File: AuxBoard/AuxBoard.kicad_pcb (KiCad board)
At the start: 2 copper layers, 85.2 x 59.2 mm, 18 parts, among them J1 ATX-24, J10 MatBIn, J11 FanHeader, J2 RPI4B, J3 Passthrough, J4 MatrixASupply, J5 MatrixBSupply, J6 BigLED, J7 MatAOut, J8 MatAIn, J9 MatBOut, U1 74125

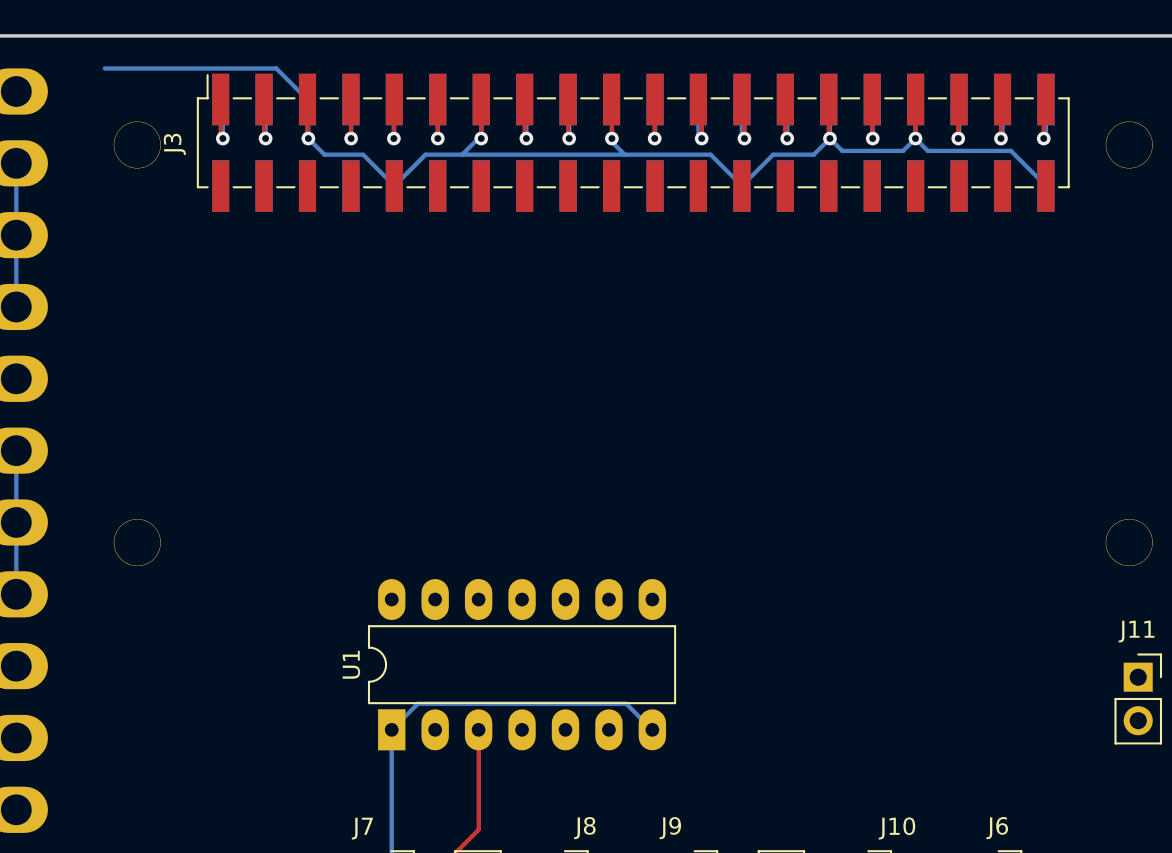
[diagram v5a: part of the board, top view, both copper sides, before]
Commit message: Simulated Ideal Diode to check functionality. Swaped Tristate buffer for hex inverter. Swapped to passthrough footprint.
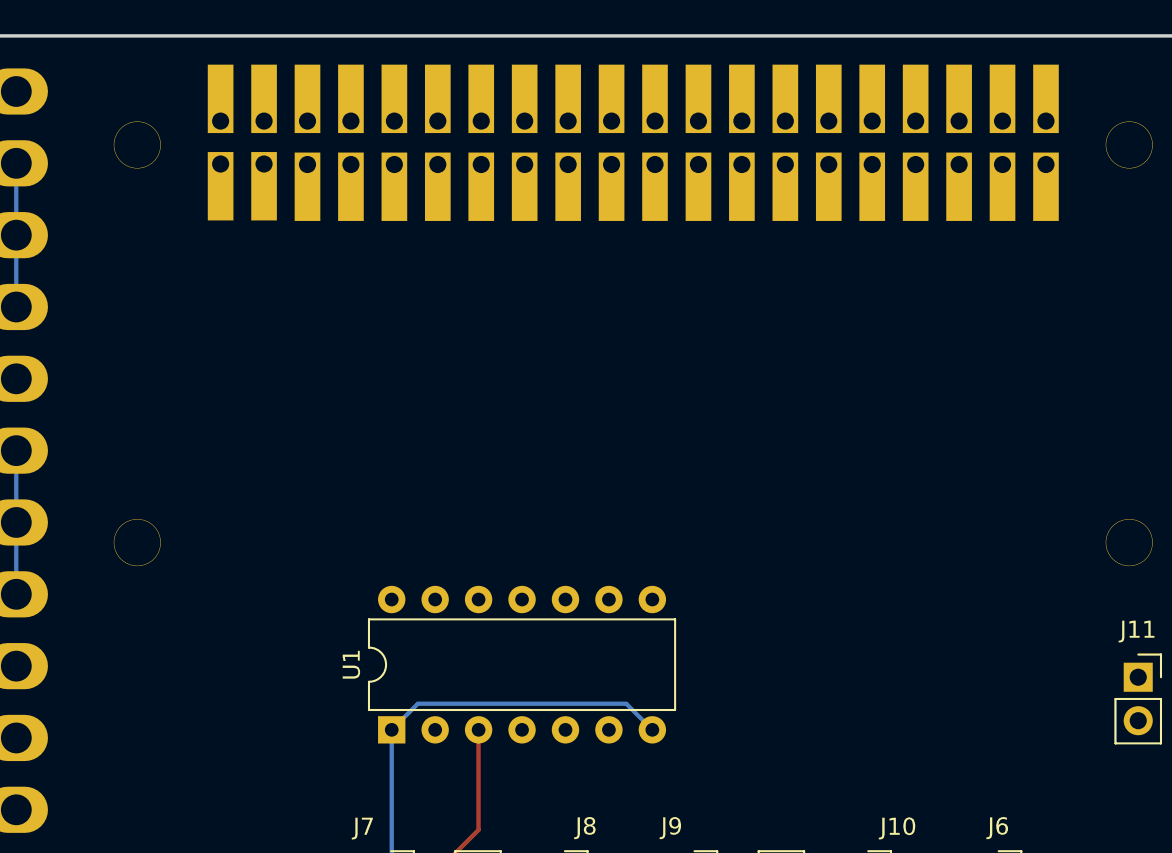
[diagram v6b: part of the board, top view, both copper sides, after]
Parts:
- removed J3: Passthrough, Connector_PinSocket_2.54mm:PinSocket_2x20_P2.54mm_FLIPED_Vertical_SMD
- J2: footprint Connector_PinSocket_2.54mm:PinSocket_2x20_P2.54mm_Vertical_SMD -> Tom's Parts:PI Header Passthrough
- U1: value 74125 -> 74AHC04; footprint Package_DIP:DIP-14_W7.62mm_LongPads -> Package_DIP:DIP-14_W7.62mm
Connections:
- U1 pad 1: GND -> /MOSI
- U1 pad 2: /MOSI -> Net-(U1-Pad2)
- U1 pad 3: DOUT -> Net-(U1-Pad2)
- U1 pad 4: unconnected-(U1B-EN-Pad4) -> DOUT
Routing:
- net GND: track 205.3 -> 118.4 mm, vias 5 -> 0
- net /5V_Power: track 9.30 -> 0.00 mm, vias 2 -> 0
- net /GPIO_8: track 4.72 -> 0.00 mm, vias 1 -> 0
- net /GPIO_7: track 4.68 -> 0.00 mm, vias 1 -> 0
- net /GPIO_21: track 4.67 -> 0.00 mm, vias 1 -> 0
- net /GPIO_1: track 4.65 -> 0.00 mm, vias 1 -> 0
- net /GPIO_23: track 4.64 -> 0.00 mm, vias 1 -> 0
- net /GPIO_20: track 4.63 -> 0.00 mm, vias 1 -> 0
- net /GPIO_24: track 4.61 -> 0.00 mm, vias 1 -> 0
- net /GPIO_16: track 4.60 -> 0.00 mm, vias 1 -> 0
- net /GPIO_15: track 4.58 -> 0.00 mm, vias 1 -> 0
- net /GPIO_12: track 4.58 -> 0.00 mm, vias 1 -> 0
- net /GPIO_25: track 4.58 -> 0.00 mm, vias 1 -> 0
- net /GPIO_14: track 4.57 -> 0.00 mm, vias 1 -> 0
- net /GPIO_18: track 4.56 -> 0.00 mm, vias 1 -> 0

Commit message: Final PCB Layout
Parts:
- removed REF** (x6): MountingHole_2.75mm_RPI_HAT, MountingHole:MountingHole_2.75mm_RPI_HAT
- added H1: MountingHole, Tom's Parts:MountingHole_2.75mm_RPI_HAT, F.Cu at (128.5, 105.4)
- added H2: MountingHole, Tom's Parts:MountingHole_2.75mm_RPI_HAT, F.Cu at (128.5, 79.4)
- added H3: MountingHole, Tom's Parts:MountingHole_2.75mm_RPI_HAT, F.Cu at (186.5, 105.4)
- added H4: MountingHole, Tom's Parts:MountingHole_2.75mm_RPI_HAT, F.Cu at (186.5, 79.4)
- added H5: MountingHole, Tom's Parts:MountingHole_2.75mm_RPI_HAT, F.Cu at (128.5, 56.1)
- added H6: MountingHole, Tom's Parts:MountingHole_2.75mm_RPI_HAT, F.Cu at (186.5, 56.1)
- added PolyFuse2: 5A, Fuse:Fuse_2920_7451Metric_Pad2.10x5.45mm_HandSolder, F.Cu at (142.8, 89.0)
- added PolyFuse3: 5A, Fuse:Fuse_2920_7451Metric_Pad2.10x5.45mm_HandSolder, F.Cu at (160.4, 89.0)
- added PolyFuse4: 3A, Fuse:Fuse_2920_7451Metric_Pad2.10x5.45mm_HandSolder, F.Cu at (176.7, 89.0)
- added PolyFuse5: 2A, Fuse:Fuse_1812_4532Metric_Pad1.30x3.40mm_HandSolder, F.Cu at (137.8, 73.1)
- added Q1: DMMT5401, Package_TO_SOT_SMD:SOT-23-6, F.Cu at (147.2, 68.2)
- added Q2: DMG2305UX, Package_TO_SOT_SMD:SOT-23-3, F.Cu at (147.2, 64.5)
- added Q3: DMG2305UX, Package_TO_SOT_SMD:SOT-23-3, F.Cu at (133.8, 68.1)
- added Q4: DMG2305UX, Package_TO_SOT_SMD:SOT-23-3, F.Cu at (186.9, 96.6)
- added R1: 10K, Resistor_SMD:R_0805_2012Metric_Pad1.20x1.40mm_HandSolder, F.Cu at (138.5, 68.2)
- added R2: 47K, Resistor_SMD:R_0805_2012Metric_Pad1.20x1.40mm_HandSolder, F.Cu at (140.5, 68.2)
- added R3: 10K, Resistor_SMD:R_0805_2012Metric_Pad1.20x1.40mm_HandSolder, F.Cu at (136.6, 68.2)
- added SW1: SW_DPST, Connector_PinHeader_2.54mm:PinHeader_2x02_P2.54mm_Vertical, F.Cu at (106.8, 104.4)
- moved U1 13.8 mm to (151.0, 78.8)
- moved J10 7.99 mm to (164.4, 102.8), turned to 180 degrees
- moved J8 7.57 mm to (147.1, 102.8), turned to 180 degrees
- moved J9 6.54 mm to (156.0, 102.8), turned to 180 degrees
- moved J7 6.49 mm to (138.3, 102.8), turned to 180 degrees
- moved J5 6.01 mm to (160.2, 100.3), turned to 0 degrees
- moved J4 5.74 mm to (142.8, 100.3), turned to 0 degrees
- moved J6 4.64 mm to (176.7, 102.8), turned to 180 degrees
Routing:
- net /5VSwitch: track 0.00 -> 207.1 mm, vias 0 -> 2
- net GND: track 118.4 -> 278.1 mm, vias 0 -> 1
- net +12V: track 4.20 -> 153.1 mm, vias 0 -> 2
- net +5V: track 33.5 -> 125.7 mm, vias 0 -> 1
- net DOUT: track 13.1 -> 51.6 mm
- net Net-(J1-PS_ON#): track 0.00 -> 35.4 mm
- net /5V_Power: track 0.00 -> 27.3 mm, vias 0 -> 2
- net +5VP: track 0.00 -> 26.7 mm
- net /3V3_Power: track 0.00 -> 26.3 mm
- net /MOSI: track 0.00 -> 26.2 mm
- net 5VSB: track 0.00 -> 22.9 mm, vias 0 -> 1
- net Net-(Q1A-E1): track 0.00 -> 20.4 mm
- net Net-(Q1B-C2): track 0.00 -> 14.1 mm
- net Net-(Q1A-B1): track 0.00 -> 10.5 mm
- net 5VMatA: track 12.3 -> 22.1 mm
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
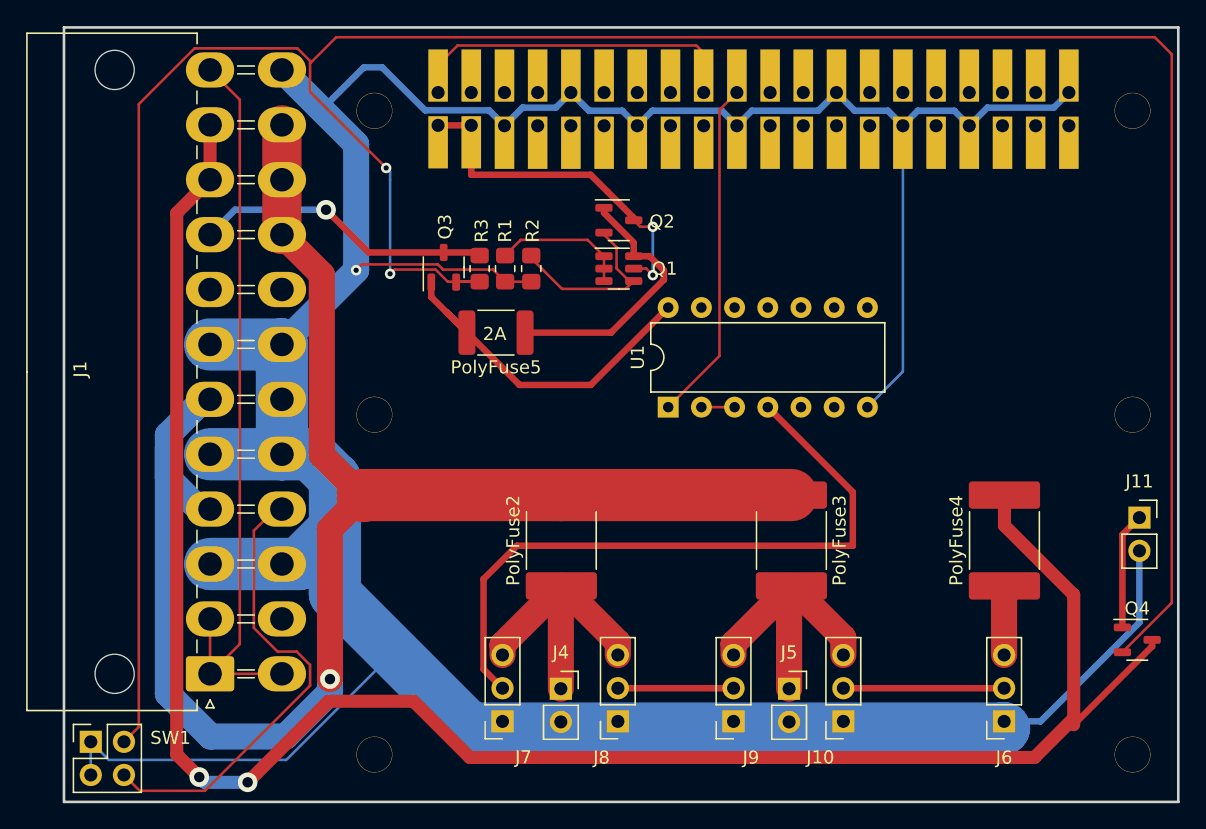
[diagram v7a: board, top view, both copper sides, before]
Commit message: Filled GND Net. Fixed most 3d elements
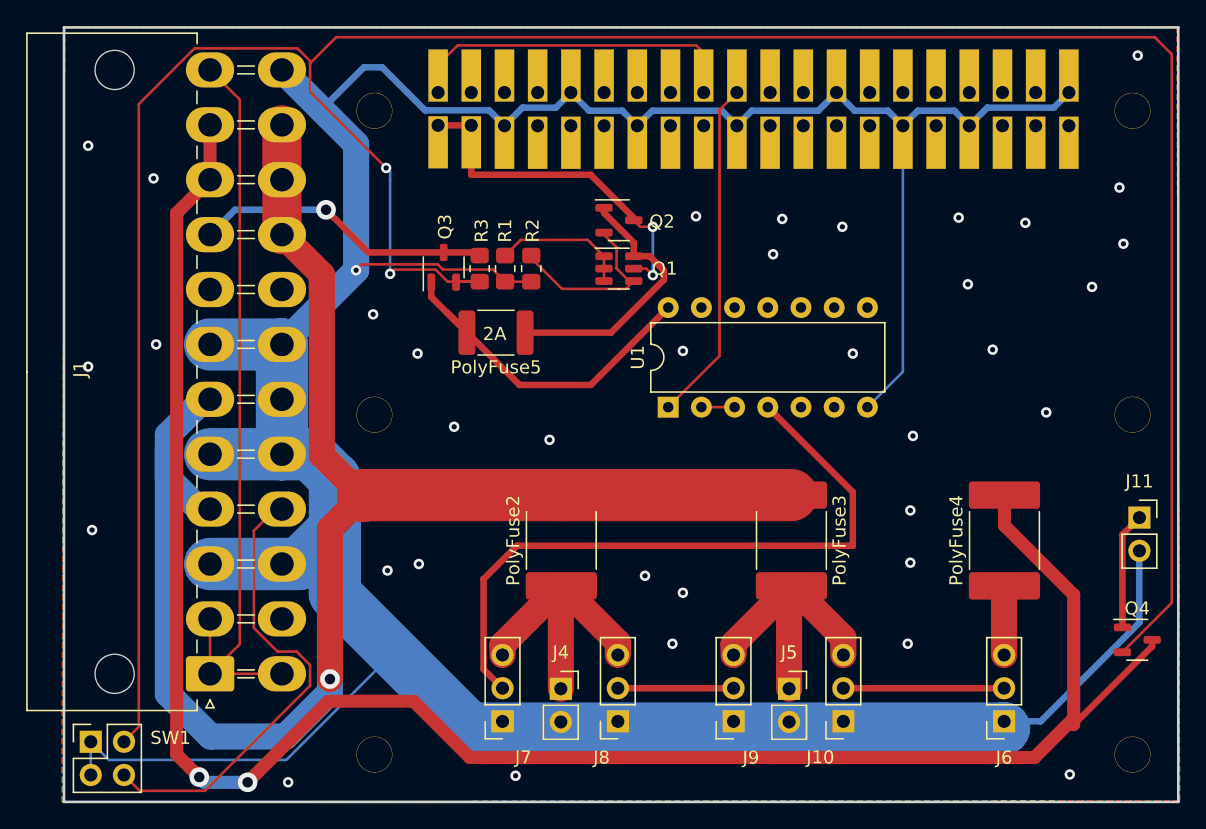
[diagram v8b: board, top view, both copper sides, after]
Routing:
- net GND: vias 1 -> 37
- added copper zone on B.Cu, net GND
- added copper zone on F.Cu, net GND
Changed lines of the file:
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@@
     (pad "2" smd roundrect (at 2.225 0 180) (size 1.3 3.4) (layers "F.Cu" "F.Paste" "F.Mask") (roundrect_rratio 0.192308)
       (net 49 "+5VP") (pintype "passive"))
-    (model "${KICAD6_3DMODEL_DIR}/Fuse.3dshapes/Fuse_1812_4532Metric.wrl"
+    (model "${KICAD7_3DMODEL_DIR}/Fuse.3dshapes/Fuse_1210_3225Metric.wrl"
       (offset (xyz 0 0 0))
       (scale (xyz 1 1 1))
@@
         (effects (font (size 1 1) (thickness 0.15)))
     )
-    (fp_text user "${REFERENCE}" (at 0 0 -90) (layer "F.Fab")
+    (fp_text user "${REFERENCE}" (at 0 0 90) (layer "F.Fab")
         (effects (font (size 1 1) (thickness 0.15)))
     )
@@
     (pad "2" smd roundrect (at 3.475 0 270) (size 2.1 5.45) (layers "F.Cu" "F.Paste" "F.Mask") (roundrect_rratio 0.119048)
       (net 46 "5VMatB") (pintype "passive"))
-    (model "${KICAD6_3DMODEL_DIR}/Fuse.3dshapes/Fuse_2920_7451Metric.wrl"
+    (model "${KICAD7_3DMODEL_DIR}/Fuse.3dshapes/Fuse_1210_3225Metric.wrl"
       (offset (xyz 0 0 0))
       (scale (xyz 1 1 1))
@@
     (pad "3" smd roundrect (at 1.1375 0) (size 1.325 0.6) (layers "F.Cu" "F.Paste" "F.Mask") (roundrect_rratio 0.25)
       (net 6 "/5V_Power") (pinfunction "S") (pintype "passive"))
-    (model "${KICAD6_3DMODEL_DIR}/Package_TO_SOT_SMD.3dshapes/SOT-23-3.wrl"
+    (model "${KICAD6_3DMODEL_DIR}/Package_TO_SOT_SMD.3dshapes/SOT-23.wrl"
       (offset (xyz 0 0 0))
       (scale (xyz 1 1 1))
@@
     (pad "3" smd roundrect (at 1.1375 0 90) (size 1.325 0.6) (layers "F.Cu" "F.Paste" "F.Mask") (roundrect_rratio 0.25)
       (net 32 "5VSB") (pinfunction "S") (pintype "passive"))
-    (model "${KICAD6_3DMODEL_DIR}/Package_TO_SOT_SMD.3dshapes/SOT-23-3.wrl"
+    (model "${KICAD6_3DMODEL_DIR}/Package_TO_SOT_SMD.3dshapes/SOT-23.wrl"
       (offset (xyz 0 0 0))
       (scale (xyz 1 1 1))
@@
     (pad "2" smd roundrect (at 3.475 0 90) (size 2.1 5.45) (layers "F.Cu" "F.Paste" "F.Mask") (roundrect_rratio 0.119048)
       (net 33 "+12V") (pintype "passive"))
-    (model "${KICAD6_3DMODEL_DIR}/Fuse.3dshapes/Fuse_2920_7451Metric.wrl"
+    (model "${KICAD7_3DMODEL_DIR}/Fuse.3dshapes/Fuse_1210_3225Metric.wrl"
       (offset (xyz 0 0 0))
       (scale (xyz 1 1 1))
@@
     (pad "2" smd roundrect (at 3.475 0 90) (size 2.1 5.45) (layers "F.Cu" "F.Paste" "F.Mask") (roundrect_rratio 0.119048)
       (net 30 "+5V") (pintype "passive"))
-    (model "${KICAD6_3DMODEL_DIR}/Fuse.3dshapes/Fuse_2920_7451Metric.wrl"
+    (model "${KICAD7_3DMODEL_DIR}/Fuse.3dshapes/Fuse_1210_3225Metric.wrl"
       (offset (xyz 0 0 0))
       (scale (xyz 1 1 1))
@@
     (pad "3" smd roundrect (at 1.1375 0) (size 1.325 0.6) (layers "F.Cu" "F.Paste" "F.Mask") (roundrect_rratio 0.25)
       (net 33 "+12V") (pinfunction "S") (pintype "passive"))
-    (model "${KICAD6_3DMODEL_DIR}/Package_TO_SOT_SMD.3dshapes/SOT-23-3.wrl"
+    (model "${KICAD7_3DMODEL_DIR}/Package_TO_SOT_SMD.3dshapes/SOT-23.wrl"
       (offset (xyz 0 0 0))
       (scale (xyz 1 1 1))
@@
   (segment (start 127.549501 67.875499) (end 127.1 68.325) (width 0.2) (layer "F.Cu") (net 48))
   (segment (start 138.5 69.2) (end 137.575 68.275) (width 0.2) (layer "F.Cu") (net 48))
+  (via (at 178.3 64.7) (size 0.8) (drill 0.4) (layers "F.Cu" "B.Cu") (free) (net 48))
+  (via (at 181.7 106.9) (size 0.8) (drill 0.4) (layers "F.Cu" "B.Cu") (free) (net 48))
+  (via (at 169.5 90.7) (size 0.8) (drill 0.4) (layers "F.Cu" "B.Cu") (free) (net 48))
+  (via (at 183.4 69.6) (size 0.8) (drill 0.4) (layers "F.Cu" "B.Cu") (free) (net 48))
+  (via (at 134.6 80.3) (size 0.8) (drill 0.4) (layers "F.Cu" "B.Cu") (free) (net 48))
   (via (at 127.1 68.325) (size 0.8) (drill 0.4) (layers "F.Cu" "B.Cu") (net 48))
+  (via (at 131.9 90.8) (size 0.8) (drill 0.4) (layers "F.Cu" "B.Cu") (free) (net 48))
+  (via (at 128.4 71.7) (size 0.8) (drill 0.4) (layers "F.Cu" "B.Cu") (free) (net 48))
+  (via (at 152.1 93) (size 0.8) (drill 0.4) (layers "F.Cu" "B.Cu") (free) (net 48))
+  (via (at 152.1 74.5) (size 0.8) (drill 0.4) (layers "F.Cu" "B.Cu") (free) (net 48))
+  (via (at 165.1 74.7) (size 0.8) (drill 0.4) (layers "F.Cu" "B.Cu") (free) (net 48))
+  (via (at 179.9 79.2) (size 0.8) (drill 0.4) (layers "F.Cu" "B.Cu") (free) (net 48))
+  (via (at 106.6 75.7) (size 0.8) (drill 0.4) (layers "F.Cu" "B.Cu") (free) (net 48))
+  (via (at 151.3 96.9) (size 0.8) (drill 0.4) (layers "F.Cu" "B.Cu") (free) (net 48))
+  (via (at 131.8 74.7) (size 0.8) (drill 0.4) (layers "F.Cu" "B.Cu") (free) (net 48))
+  (via (at 185.8 66.3) (size 0.8) (drill 0.4) (layers "F.Cu" "B.Cu") (free) (net 48))
+  (via (at 173.2 64.3) (size 0.8) (drill 0.4) (layers "F.Cu" "B.Cu") (free) (net 48))
+  (via (at 111.6 61.3) (size 0.8) (drill 0.4) (layers "F.Cu" "B.Cu") (free) (net 48))
+  (via (at 175.8 74.4) (size 0.8) (drill 0.4) (layers "F.Cu" "B.Cu") (free) (net 48))
+  (via (at 159 67.1) (size 0.8) (drill 0.4) (layers "F.Cu" "B.Cu") (free) (net 48))
+  (via (at 169.7 81) (size 0.8) (drill 0.4) (layers "F.Cu" "B.Cu") (free) (net 48))
+  (via (at 169.5 86.7) (size 0.8) (drill 0.4) (layers "F.Cu" "B.Cu") (free) (net 48))
+  (via (at 169.3 96.9) (size 0.8) (drill 0.4) (layers "F.Cu" "B.Cu") (free) (net 48))
+  (via (at 141.9 81.3) (size 0.8) (drill 0.4) (layers "F.Cu" "B.Cu") (free) (net 48))
+  (via (at 106.6 58.8) (size 0.8) (drill 0.4) (layers "F.Cu" "B.Cu") (free) (net 48))
+  (via (at 129.5 91.3) (size 0.8) (drill 0.4) (layers "F.Cu" "B.Cu") (free) (net 48))
+  (via (at 149.2 91.7) (size 0.8) (drill 0.4) (layers "F.Cu" "B.Cu") (free) (net 48))
+  (via (at 164.3 65) (size 0.8) (drill 0.4) (layers "F.Cu" "B.Cu") (free) (net 48))
+  (via (at 106.9 88.2) (size 0.8) (drill 0.4) (layers "F.Cu" "B.Cu") (free) (net 48))
+  (via (at 111.8 74) (size 0.8) (drill 0.4) (layers "F.Cu" "B.Cu") (free) (net 48))
+  (via (at 139.3 107) (size 0.8) (drill 0.4) (layers "F.Cu" "B.Cu") (free) (net 48))
+  (via (at 121.9 107.5) (size 0.8) (drill 0.4) (layers "F.Cu" "B.Cu") (free) (net 48))
+  (via (at 153.1 64.2) (size 0.8) (drill 0.4) (layers "F.Cu" "B.Cu") (free) (net 48))
+  (via (at 159.7 64.4) (size 0.8) (drill 0.4) (layers "F.Cu" "B.Cu") (free) (net 48))
+  (via (at 186.9 51.9) (size 0.8) (drill 0.4) (layers "F.Cu" "B.Cu") (free) (net 48))
+  (via (at 185.5 62) (size 0.8) (drill 0.4) (layers "F.Cu" "B.Cu") (free) (net 48))
+  (via (at 173.9 69.4) (size 0.8) (drill 0.4) (layers "F.Cu" "B.Cu") (free) (net 48))
   (segment (start 121.425 82.4) (end 115.925 82.4) (width 4) (layer "B.Cu") (net 48))
   (segment (start 156.23 57.27) (end 157.38 56.12) (width 0.5) (layer "B.Cu") (net 48))
@@
   (segment (start 129.7 60.8) (end 129.4 60.5) (width 0.2) (layer "B.Cu") (net 60))
   (segment (start 129.7 61.4) (end 129.7 60.8) (width 0.2) (layer "B.Cu") (net 60))
+  (zone (net 48) (net_name "GND") (layers "F&B.Cu") (hatch edge 0.5)
+    (connect_pads (clearance 0.5))
+    (min_thickness 0.25) (filled_areas_thickness no)
+    (fill yes (mode hatch) (thermal_gap 0.5) (thermal_bridge_width 0.5)
+      (hatch_thickness 1) (hatch_gap 1.5) (hatch_orientation 0)
+      (hatch_border_algorithm hatch_thickness) (hatch_min_hole_area 0.3))
+    (polygon
+      (pts
+        (xy 104.8 49.7)
+        (xy 189.9 49.7)
+        (xy 190.1 108.9)
+        (xy 104.6 109)
+        (xy 104.8 49.7)
+      )
+    )
+  )
   (group "" (id 5455b699-a110-4c5c-b8cd-7ac3f47d386e)
     (members
